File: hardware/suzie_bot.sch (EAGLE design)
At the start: 37 parts, among them IC1 LT1529CT33, IC2 L9637D, IC3 IC_TXB0108-TSSOP-20, U1 ATMEGA1284P-AU, Y1 14.7456, Y2 6.0, Y3 16.0

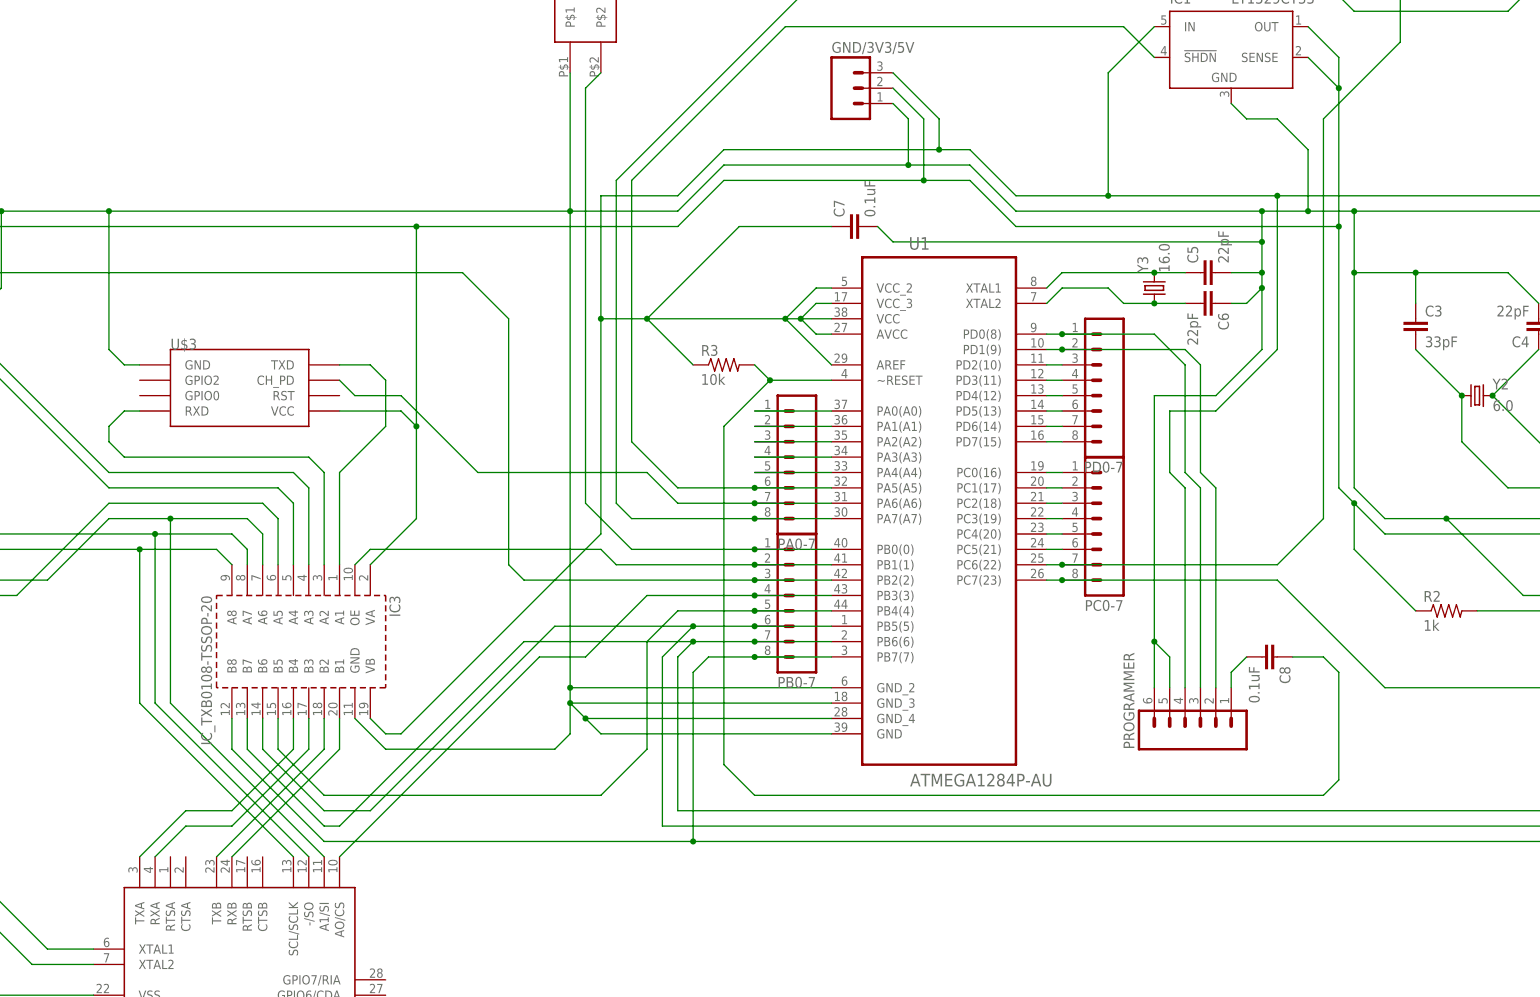
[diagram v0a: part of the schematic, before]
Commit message: Adding LED to PB1 (per https://www.flickr.com/photos/maniacbug/6413368937/)
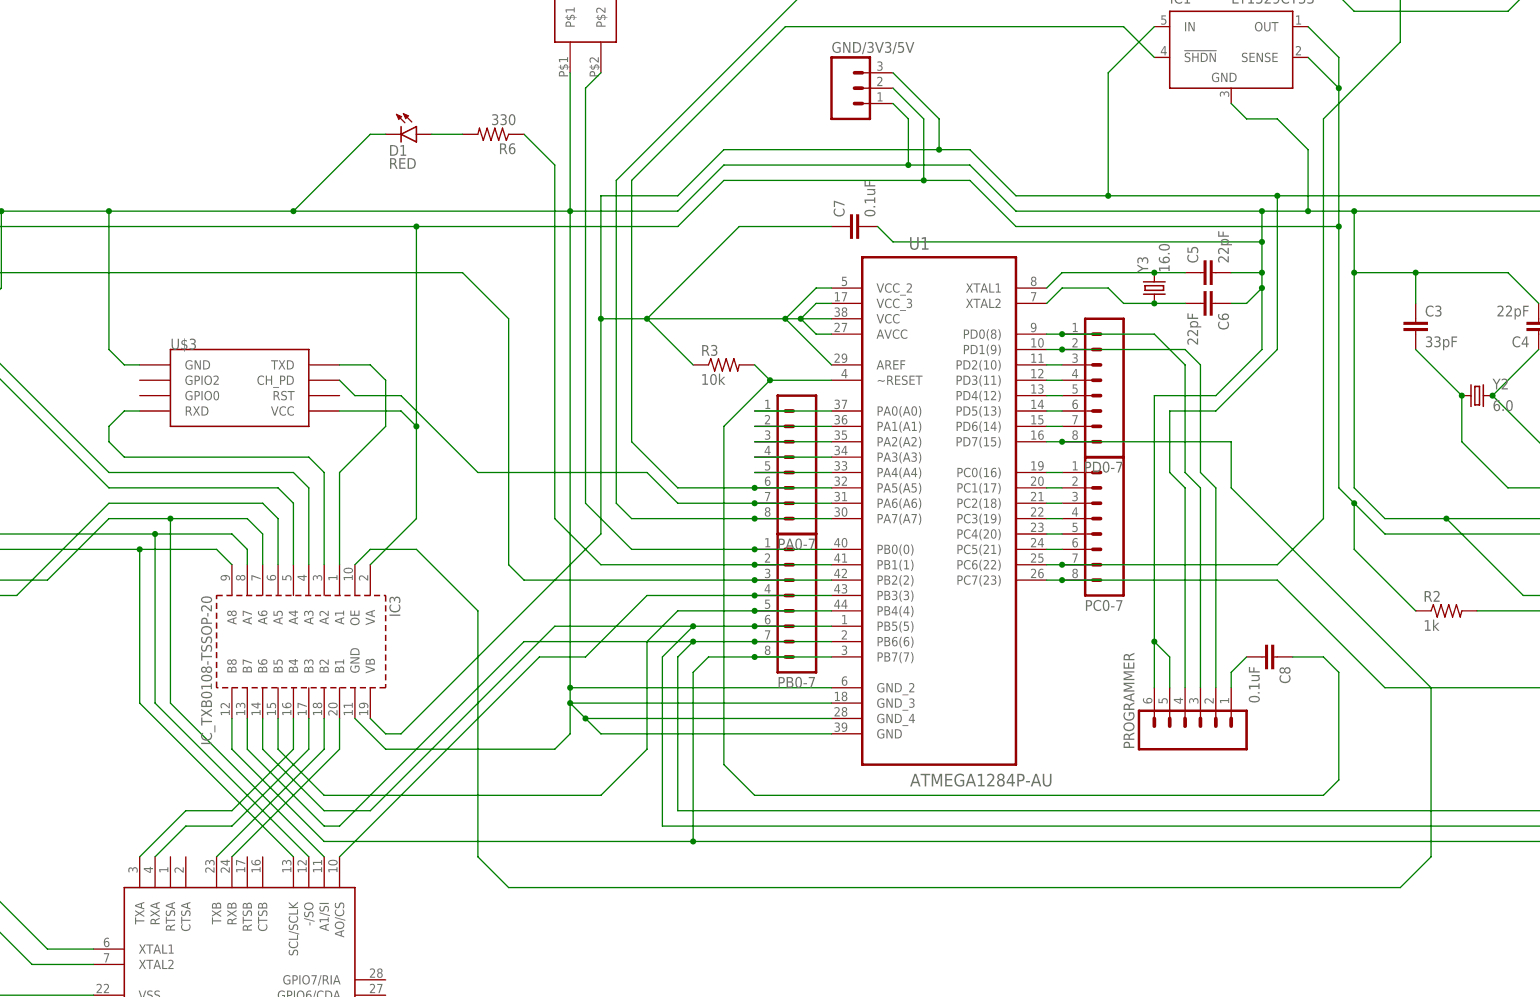
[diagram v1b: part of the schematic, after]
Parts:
- added D1: RED, SparkFun-LED:LED5MM
- added R6: 330, SparkFun-Passives:RESISTOR0805-RES
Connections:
- removed net PB1: IC3.OE, PB0-7.2, U1.PB1(1)
- new net N$2: PB0-7.2, R6.1, U1.PB1(1)
- new net N$25: D1.A, R6.2
- net GND: now also D1.C
- net PD7: now also IC3.OE
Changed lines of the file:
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@@
 <part name="R5" library="SparkFun-Passives" deviceset="RESISTOR" device="0805-RES" value="50k"/>
 <part name="U$1" library="dp_devices.v6" deviceset="CON_MICROSD" device="HINGED"/>
+<part name="D1" library="SparkFun-LED" deviceset="LED" device="5MM" value="RED"/>
+<part name="R6" library="SparkFun-Passives" deviceset="RESISTOR" device="0805-RES" value="330"/>
 </parts>
 <sheets>
@@
 <instance part="R5" gate="G$1" x="116.84" y="236.22"/>
 <instance part="U$1" gate="CON" x="-167.64" y="139.7" rot="R180"/>
+<instance part="D1" gate="G$1" x="-76.2" y="208.28" rot="R270"/>
+<instance part="R6" gate="G$1" x="-63.5" y="208.28" rot="R180"/>
 </instances>
 <busses>
@@
 <segment>
 <wire x1="-33.02" y1="195.58" x2="-50.8" y2="195.58" width="0.1524" layer="91"/>
-<wire x1="-50.8" y1="195.58" x2="-127" y2="195.58" width="0.1524" layer="91"/>
+<wire x1="-50.8" y1="195.58" x2="-96.52" y2="195.58" width="0.1524" layer="91"/>
+<wire x1="-96.52" y1="195.58" x2="-127" y2="195.58" width="0.1524" layer="91"/>
 <wire x1="-127" y1="195.58" x2="-144.78" y2="195.58" width="0.1524" layer="91"/>
 <wire x1="-144.78" y1="195.58" x2="-182.88" y2="195.58" width="0.1524" layer="91"/>
@@
 <wire x1="5.08" y1="210.82" x2="5.08" y2="203.2" width="0.1524" layer="91"/>
 <junction x="5.08" y="203.2"/>
+<pinref part="D1" gate="G$1" pin="C"/>
+<wire x1="-81.28" y1="208.28" x2="-83.82" y2="208.28" width="0.1524" layer="91"/>
+<wire x1="-83.82" y1="208.28" x2="-96.52" y2="195.58" width="0.1524" layer="91"/>
+<junction x="-96.52" y="195.58"/>
 </segment>
 </net>
@@
 </segment>
 </net>
-<net name="PB1" class="0">
-<segment>
-<pinref part="U1" gate="A" pin="PB1(1)"/>
-<pinref part="PB0-7" gate="G$1" pin="2"/>
-<wire x1="-7.62" y1="137.16" x2="-20.32" y2="137.16" width="0.1524" layer="91"/>
-<pinref part="IC3" gate="IC" pin="OE"/>
-<wire x1="-86.36" y1="137.16" x2="-83.82" y2="139.7" width="0.1524" layer="91"/>
-<wire x1="-83.82" y1="139.7" x2="-45.72" y2="139.7" width="0.1524" layer="91"/>
-<wire x1="-45.72" y1="139.7" x2="-43.18" y2="137.16" width="0.1524" layer="91"/>
-<wire x1="-43.18" y1="137.16" x2="-20.32" y2="137.16" width="0.1524" layer="91"/>
-<junction x="-20.32" y="137.16"/>
-</segment>
-</net>
 <net name="PB2" class="0">
 <segment>
@@
 <pinref part="U1" gate="A" pin="PD7(15)"/>
 <wire x1="27.94" y1="157.48" x2="30.48" y2="157.48" width="0.1524" layer="91"/>
+<pinref part="IC3" gate="IC" pin="OE"/>
+<wire x1="-86.36" y1="137.16" x2="-83.82" y2="139.7" width="0.1524" layer="91"/>
+<wire x1="-83.82" y1="139.7" x2="-76.2" y2="139.7" width="0.1524" layer="91"/>
+<wire x1="-76.2" y1="139.7" x2="-66.04" y2="129.54" width="0.1524" layer="91"/>
+<wire x1="-66.04" y1="129.54" x2="-66.04" y2="88.9" width="0.1524" layer="91"/>
+<wire x1="-66.04" y1="88.9" x2="-60.96" y2="83.82" width="0.1524" layer="91"/>
+<wire x1="-60.96" y1="83.82" x2="86.36" y2="83.82" width="0.1524" layer="91"/>
+<wire x1="86.36" y1="83.82" x2="91.44" y2="88.9" width="0.1524" layer="91"/>
+<wire x1="91.44" y1="88.9" x2="91.44" y2="116.84" width="0.1524" layer="91"/>
+<wire x1="91.44" y1="116.84" x2="58.42" y2="149.86" width="0.1524" layer="91"/>
+<wire x1="58.42" y1="149.86" x2="58.42" y2="157.48" width="0.1524" layer="91"/>
+<wire x1="58.42" y1="157.48" x2="30.48" y2="157.48" width="0.1524" layer="91"/>
+<junction x="30.48" y="157.48"/>
 </segment>
 </net>
@@
 </segment>
 </net>
+<net name="N$2" class="0">
+<segment>
+<pinref part="PB0-7" gate="G$1" pin="2"/>
+<pinref part="U1" gate="A" pin="PB1(1)"/>
+<wire x1="-7.62" y1="137.16" x2="-20.32" y2="137.16" width="0.1524" layer="91"/>
+<wire x1="-20.32" y1="137.16" x2="-45.72" y2="137.16" width="0.1524" layer="91"/>
+<junction x="-20.32" y="137.16"/>
+<wire x1="-45.72" y1="137.16" x2="-53.34" y2="144.78" width="0.1524" layer="91"/>
+<wire x1="-53.34" y1="144.78" x2="-53.34" y2="203.2" width="0.1524" layer="91"/>
+<pinref part="R6" gate="G$1" pin="1"/>
+<wire x1="-53.34" y1="203.2" x2="-58.42" y2="208.28" width="0.1524" layer="91"/>
+</segment>
+</net>
+<net name="N$25" class="0">
+<segment>
+<pinref part="D1" gate="G$1" pin="A"/>
+<pinref part="R6" gate="G$1" pin="2"/>
+<wire x1="-73.66" y1="208.28" x2="-68.58" y2="208.28" width="0.1524" layer="91"/>
+</segment>
+</net>
